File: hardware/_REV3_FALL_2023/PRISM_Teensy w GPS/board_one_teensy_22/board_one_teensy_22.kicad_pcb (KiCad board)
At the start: 2 copper layers, 61 x 88.9 mm, 32 parts, among them J1 Micro_SD_Card_Det_Hirose_DM3AT, J3 3387, Q1 AO3400A, Q2 AO3400A, U1 Teensy4.0, U2 GPS-14414, U3 3966, U4 RFM69HCW_Breakout, U5 CT25E-16T150-1, U6 CMI-9605-1280T

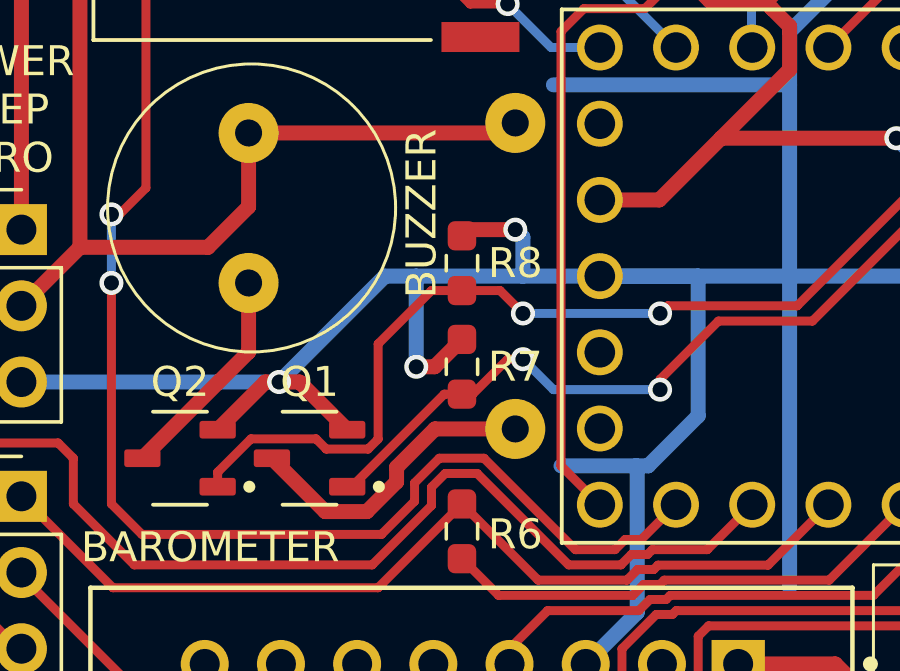
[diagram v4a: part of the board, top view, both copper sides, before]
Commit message: Move resistors out of solder iron path
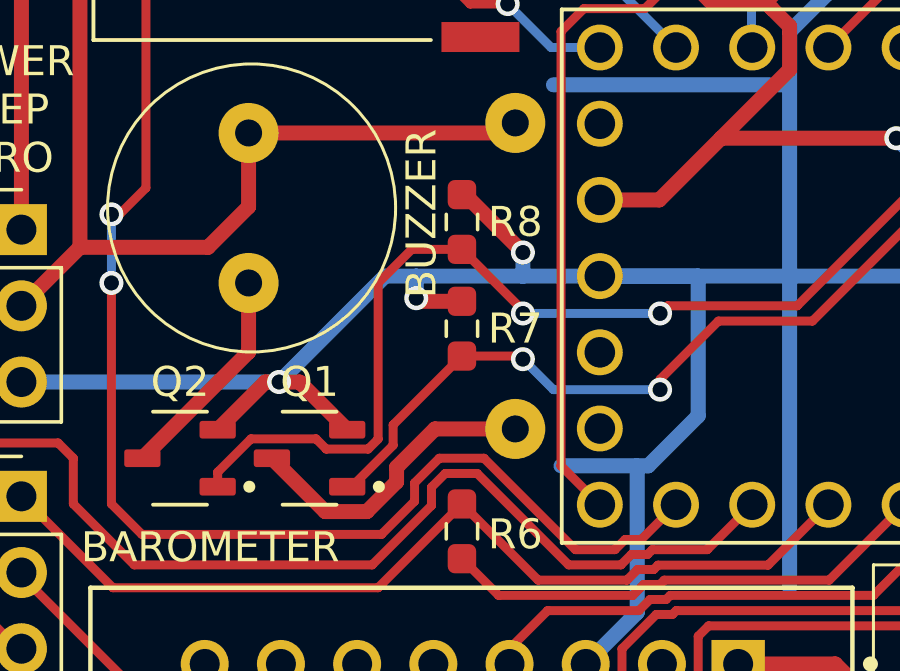
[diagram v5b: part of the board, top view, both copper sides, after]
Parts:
- moved R8 1.37 mm to (126.0, 102.6)
- moved R7 1.27 mm to (126.0, 106.2)
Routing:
- net GND: track 286.7 -> 284.1 mm
- net /BUZZER 2: track 37.1 -> 39.5 mm
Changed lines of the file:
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@@
   )
   (footprint "Resistor_SMD:R_0603_1608Metric_Pad0.98x0.95mm_HandSolder" (layer "F.Cu")
-    (at 125.984 107.442 -90)
+    (at 125.984 106.172 -90)
     (descr "Resistor SMD 0603 (1608 Metric), square (rectangular) end terminal, IPC_7351 nominal with elongated pad for handsoldering. (Body size source: IPC-SM-782 page 72, https://www.pcb-3d.com/wordpress/wp-content/uploads/ipc-sm-782a_amendment_1_and_2.pdf), generated with kicad-footprint-generator")
     (tags "resistor handsolder")
@@
   )
   (footprint "Resistor_SMD:R_0603_1608Metric_Pad0.98x0.95mm_HandSolder" (layer "F.Cu")
-    (at 125.984 103.9895 -90)
+    (at 125.984 102.616 -90)
     (descr "Resistor SMD 0603 (1608 Metric), square (rectangular) end terminal, IPC_7351 nominal with elongated pad for handsoldering. (Body size source: IPC-SM-782 page 72, https://www.pcb-3d.com/wordpress/wp-content/uploads/ipc-sm-782a_amendment_1_and_2.pdf), generated with kicad-footprint-generator")
     (tags "resistor handsolder")
@@
   (segment (start 131.8565 91.4095) (end 132.334 90.932) (width 0.5) (layer "F.Cu") (net 1))
   (segment (start 141.092 89.944) (end 139.728 89.944) (width 0.5) (layer "F.Cu") (net 1))
+  (segment (start 126.0875 101.7035) (end 125.984 101.7035) (width 0.5) (layer "F.Cu") (net 1))
   (segment (start 139.728 89.944) (end 139.7 89.916) (width 0.5) (layer "F.Cu") (net 1))
   (segment (start 155.29 88.254) (end 149.49 88.254) (width 0.5) (layer "F.Cu") (net 1))
@@
   (segment (start 130.0695 92.15) (end 127.1 92.15) (width 0.5) (layer "F.Cu") (net 1))
   (segment (start 130.81 91.4095) (end 130.0695 92.15) (width 0.5) (layer "F.Cu") (net 1))
-  (segment (start 126.191 102.87) (end 125.984 103.077) (width 0.5) (layer "F.Cu") (net 1))
+  (segment (start 128.016 103.632) (end 126.0875 101.7035) (width 0.5) (layer "F.Cu") (net 1))
   (segment (start 120.569 107.95) (end 122.159 109.54) (width 0.5) (layer "F.Cu") (net 1))
   (segment (start 119.431 107.95) (end 117.841 109.54) (width 0.5) (layer "F.Cu") (net 1))
+  (segment (start 124.46 105.156) (end 124.5635 105.2595) (width 0.5) (layer "F.Cu") (net 1))
   (segment (start 139.7 89.916) (end 139.7 88.646) (width 0.5) (layer "F.Cu") (net 1))
-  (segment (start 124.46 107.442) (end 125.0715 107.442) (width 0.5) (layer "F.Cu") (net 1))
-  (segment (start 125.0715 107.442) (end 125.984 106.5295) (width 0.5) (layer "F.Cu") (net 1))
-  (segment (start 127.762 102.87) (end 126.191 102.87) (width 0.5) (layer "F.Cu") (net 1))
-  (via (at 124.46 107.442) (size 0.8) (drill 0.5) (layers "F.Cu" "B.Cu") (net 1))
+  (segment (start 124.5635 105.2595) (end 125.984 105.2595) (width 0.5) (layer "F.Cu") (net 1))
+  (via (at 124.46 105.156) (size 0.8) (drill 0.5) (layers "F.Cu" "B.Cu") (net 1))
   (via (at 132.334 90.932) (size 0.8) (drill 0.5) (layers "F.Cu" "B.Cu") (net 1))
-  (via (at 127.762 102.87) (size 0.8) (drill 0.5) (layers "F.Cu" "B.Cu") (net 1))
+  (via (at 128.016 103.632) (size 0.8) (drill 0.5) (layers "F.Cu" "B.Cu") (net 1))
   (via (at 139.7 88.646) (size 0.8) (drill 0.5) (layers "F.Cu" "B.Cu") (net 1))
   (via (at 151.638 88.254) (size 0.8) (drill 0.5) (layers "F.Cu" "B.Cu") (net 1))
@@
   (segment (start 160.362 95.416) (end 159.845 95.933) (width 0.5) (layer "B.Cu") (net 1))
   (segment (start 138.176 88.646) (end 138.176 90.932) (width 0.5) (layer "B.Cu") (net 1))
-  (segment (start 124.46 107.442) (end 124.46 104.42) (width 0.5) (layer "B.Cu") (net 1))
   (segment (start 161.06 112.04) (end 153.44 104.42) (width 0.5) (layer "B.Cu") (net 1))
+  (segment (start 128.016 103.632) (end 128.016 104.42) (width 0.5) (layer "B.Cu") (net 1))
   (segment (start 141.986 104.42) (end 144.526 104.42) (width 0.5) (layer "B.Cu") (net 1))
   (segment (start 130.11 117.348) (end 131.826 115.632) (width 0.5) (layer "B.Cu") (net 1))
-  (segment (start 128.016 103.124) (end 127.762 102.87) (width 0.5) (layer "B.Cu") (net 1))
   (segment (start 141.986 104.42) (end 141.986 113.792) (width 0.5) (layer "B.Cu") (net 1))
   (segment (start 159.766 96.012) (end 159.845 95.933) (width 0.5) (layer "B.Cu") (net 1))
@@
   (segment (start 132.1915 110.744) (end 133.858 109.0775) (width 0.5) (layer "B.Cu") (net 1))
   (segment (start 154.686 91.302) (end 154.686 102.455468) (width 0.5) (layer "B.Cu") (net 1))
-  (segment (start 128.016 104.42) (end 128.016 103.124) (width 0.5) (layer "B.Cu") (net 1))
   (segment (start 152.146 104.42) (end 152.146 114.046) (width 0.5) (layer "B.Cu") (net 1))
   (segment (start 154.686 102.455468) (end 154.605734 102.535734) (width 0.5) (layer "B.Cu") (net 1))
@@
   (segment (start 159.766 97.375468) (end 159.766 96.012) (width 0.5) (layer "B.Cu") (net 1))
   (segment (start 133.858 109.0775) (end 133.858 104.42) (width 0.5) (layer "B.Cu") (net 1))
+  (segment (start 124.46 105.156) (end 124.46 104.42) (width 0.5) (layer "B.Cu") (net 1))
   (segment (start 136.906 96.272532) (end 136.906 98.044) (width 0.5) (layer "B.Cu") (net 1))
   (segment (start 123.418 104.42) (end 119.888 107.95) (width 0.5) (layer "B.Cu") (net 1))
@@
   (segment (start 128.9575 96.8) (end 127.508 95.3505) (width 0.3) (layer "B.Cu") (net 8))
   (segment (start 132.588 107.8625) (end 134.5325 105.918) (width 0.3) (layer "F.Cu") (net 9))
-  (segment (start 127.508 107.188) (end 126.3415 108.3545) (width 0.3) (layer "F.Cu") (net 9))
-  (segment (start 128.016 107.188) (end 127.508 107.188) (width 0.3) (layer "F.Cu") (net 9))
-  (segment (start 122.30924 111.44) (end 122.159 111.44) (width 0.3) (layer "F.Cu") (net 9))
-  (segment (start 125.39474 108.3545) (end 122.30924 111.44) (width 0.3) (layer "F.Cu") (net 9))
   (segment (start 137.668 105.918) (end 144.872 98.714) (width 0.3) (layer "F.Cu") (net 9))
+  (segment (start 122.30924 111.44) (end 122.159 111.44) (width 0.3) (layer "F.Cu") (net 9))
+  (segment (start 127.9125 107.0845) (end 125.984 107.0845) (width 0.3) (layer "F.Cu") (net 9))
+  (segment (start 123.69 109.3785) (end 123.69 110.05924) (width 0.3) (layer "F.Cu") (net 9))
   (segment (start 147.595 96.8) (end 148.36 96.8) (width 0.3) (layer "F.Cu") (net 9))
+  (segment (start 123.69 110.05924) (end 122.30924 111.44) (width 0.3) (layer "F.Cu") (net 9))
+  (segment (start 128.016 107.188) (end 127.9125 107.0845) (width 0.3) (layer "F.Cu") (net 9))
   (segment (start 145.681 98.714) (end 147.595 96.8) (width 0.3) (layer "F.Cu") (net 9))
   (segment (start 134.5325 105.918) (end 137.668 105.918) (width 0.3) (layer "F.Cu") (net 9))
-  (segment (start 126.3415 108.3545) (end 125.984 108.3545) (width 0.3) (layer "F.Cu") (net 9))
   (segment (start 144.872 98.714) (end 145.681 98.714) (width 0.3) (layer "F.Cu") (net 9))
   (segment (start 132.588 108.204) (end 132.588 107.8625) (width 0.3) (layer "F.Cu") (net 9))
-  (segment (start 125.984 108.3545) (end 125.39474 108.3545) (width 0.3) (layer "F.Cu") (net 9))
+  (segment (start 125.984 107.0845) (end 123.69 109.3785) (width 0.3) (layer "F.Cu") (net 9))
   (via (at 132.588 108.204) (size 0.8) (drill 0.5) (layers "F.Cu" "B.Cu") (net 9))
   (via (at 128.016 107.188) (size 0.8) (drill 0.5) (layers "F.Cu" "B.Cu") (net 9))
@@
   (segment (start 118.872 102.108) (end 117.52 103.46) (width 0.5) (layer "F.Cu") (net 19))
   (segment (start 111.3 105.41) (end 113.25 103.46) (width 0.5) (layer "F.Cu") (net 19))
+  (segment (start 128.016 105.5605) (end 125.984 103.5285) (width 0.3) (layer "F.Cu") (net 23))
+  (segment (start 117.841 110.954866) (end 117.841 111.44) (width 0.3) (layer "F.Cu") (net 23))
   (segment (start 132.588 105.664) (end 132.842 105.41) (width 0.3) (layer "F.Cu") (net 23))
-  (segment (start 118.950866 109.845) (end 117.841 110.954866) (width 0.3) (layer "F.Cu") (net 23))
-  (segment (start 125.984 104.902) (end 124.968 104.902) (width 0.3) (layer "F.Cu") (net 23))
-  (segment (start 122.857134 110.185) (end 121.460866 110.185) (width 0.3) (layer "F.Cu") (net 23))
-  (segment (start 132.842 105.41) (end 137.16 105.41) (width 0.3) (layer "F.Cu") (net 23))
   (segment (start 121.120866 109.845) (end 118.950866 109.845) (width 0.3) (layer "F.Cu") (net 23))
-  (segment (start 137.16 105.41) (end 145.77 96.8) (width 0.3) (layer "F.Cu") (net 23))
+  (segment (start 132.842 105.41) (end 137.16 105.41) (width 0.3) (layer "F.Cu") (net 23))
+  (segment (start 123.19 109.852134) (end 122.857134 110.185) (width 0.3) (layer "F.Cu") (net 23))
+  (segment (start 123.19 104.648) (end 123.19 109.852134) (width 0.3) (layer "F.Cu") (net 23))
   (segment (start 121.460866 110.185) (end 121.120866 109.845) (width 0.3) (layer "F.Cu") (net 23))
-  (segment (start 127.254 104.902) (end 125.984 104.902) (width 0.3) (layer "F.Cu") (net 23))
-  (segment (start 123.19 106.68) (end 123.19 109.852134) (width 0.3) (layer "F.Cu") (net 23))
-  (segment (start 128.016 105.664) (end 127.254 104.902) (width 0.3) (layer "F.Cu") (net 23))
+  (segment (start 125.984 103.5285) (end 124.3095 103.5285) (width 0.3) (layer "F.Cu") (net 23))
+  (segment (start 137.16 105.41) (end 145.77 96.8) (width 0.3) (layer "F.Cu") (net 23))
+  (segment (start 122.857134 110.185) (end 121.460866 110.185) (width 0.3) (layer "F.Cu") (net 23))
   (segment (start 145.77 96.8) (end 145.82 96.8) (width 0.3) (layer "F.Cu") (net 23))
-  (segment (start 117.841 110.954866) (end 117.841 111.44) (width 0.3) (layer "F.Cu") (net 23))
-  (segment (start 124.968 104.902) (end 123.19 106.68) (width 0.3) (layer "F.Cu") (net 23))
-  (segment (start 123.19 109.852134) (end 122.857134 110.185) (width 0.3) (layer "F.Cu") (net 23))
+  (segment (start 124.3095 103.5285) (end 123.19 104.648) (width 0.3) (layer "F.Cu") (net 23))
+  (segment (start 128.016 105.664) (end 128.016 105.5605) (width 0.3) (layer "F.Cu") (net 23))
+  (segment (start 118.950866 109.845) (end 117.841 110.954866) (width 0.3) (layer "F.Cu") (net 23))
   (via (at 132.588 105.664) (size 0.8) (drill 0.5) (layers "F.Cu" "B.Cu") (net 23))
   (via (at 128.016 105.664) (size 0.8) (drill 0.5) (layers "F.Cu" "B.Cu") (net 23))

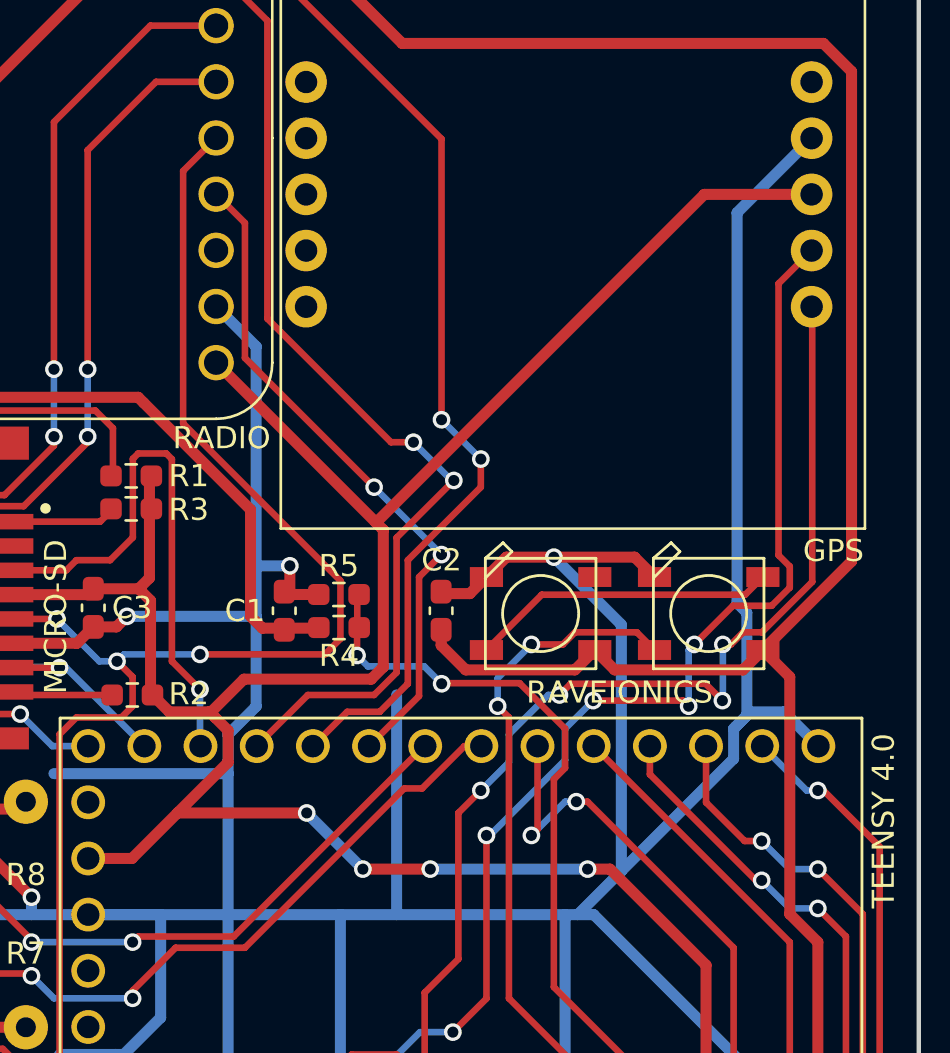
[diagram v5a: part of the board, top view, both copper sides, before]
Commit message: Fixed GPS breakout schematic pin assignment and updated board to update traces
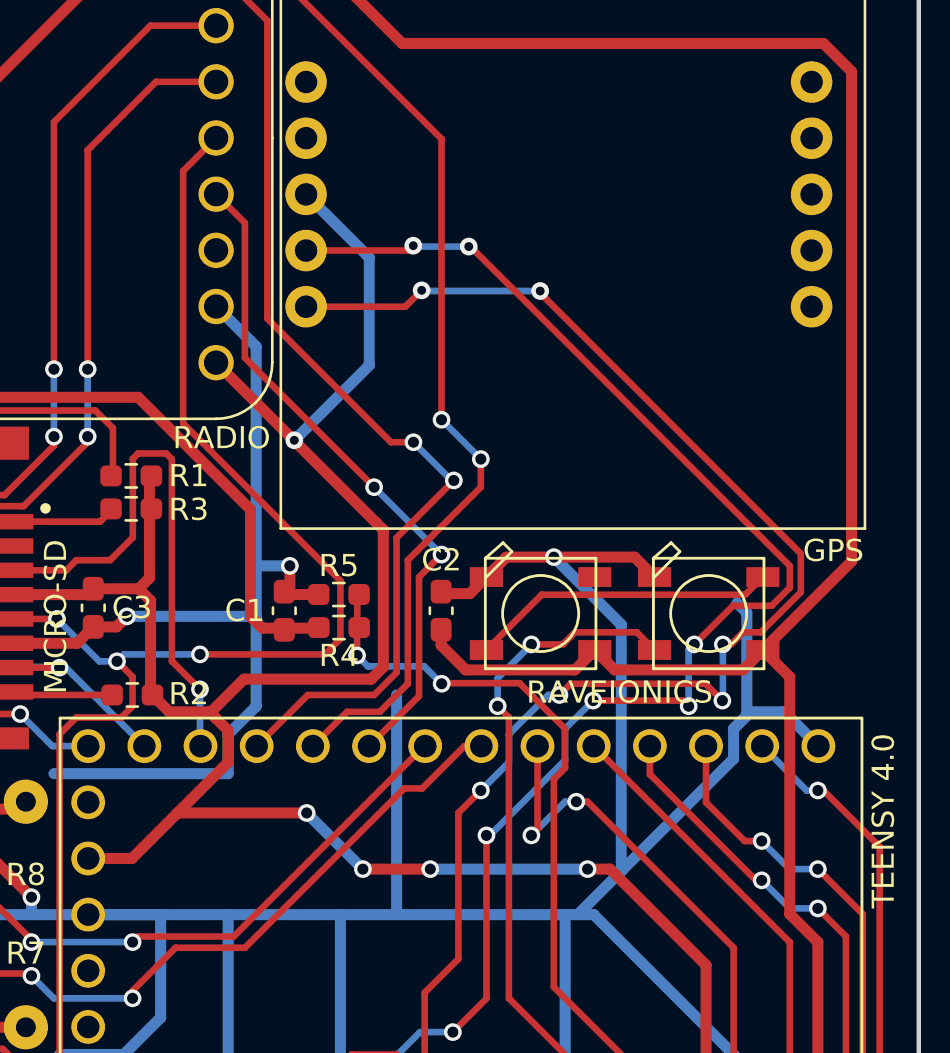
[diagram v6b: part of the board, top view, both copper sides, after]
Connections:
- U2 pad 10: unconnected-(U2-TX-Pad10) -> /SCL
- U2 pad 2: GND -> unconnected-(U2-RST-Pad2)
- U2 pad 3: /3.3V -> unconnected-(U2-PPS-Pad3)
- U2 pad 4: /SDA -> unconnected-(U2-RX-Pad4)
- U2 pad 5: /SCL -> unconnected-(U2-TX-Pad5)
- U2 pad 7: unconnected-(U2-RST-Pad7) -> GND
- U2 pad 8: unconnected-(U2-PPS-Pad8) -> /3.3V
- U2 pad 9: unconnected-(U2-RX-Pad9) -> /SDA
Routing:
- net GND: track 284.1 -> 255.4 mm
- net /SCL: track 90.2 -> 106.7 mm, vias 4 -> 6
- net /SDA: track 102.3 -> 115.4 mm, vias 5 -> 7
- net /3.3V: track 153.6 -> 141.5 mm, vias 6 -> 7

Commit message: Fixed Silkscreen and removed power plane
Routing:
- added copper zone on F.Cu, net GND
- removed copper zone on F.Cu, net /3.3V
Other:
- board text added: "Jojo Liu"
- board text added: "Rishit Bansal"
- board text removed: "Joseph Liu"
